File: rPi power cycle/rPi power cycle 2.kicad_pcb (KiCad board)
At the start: 2 copper layers, 53.3 x 25.4 mm, 9 parts, among them J1 RPi GPIO, J2 BATT, J3 RPi PWR, Q1 BC548

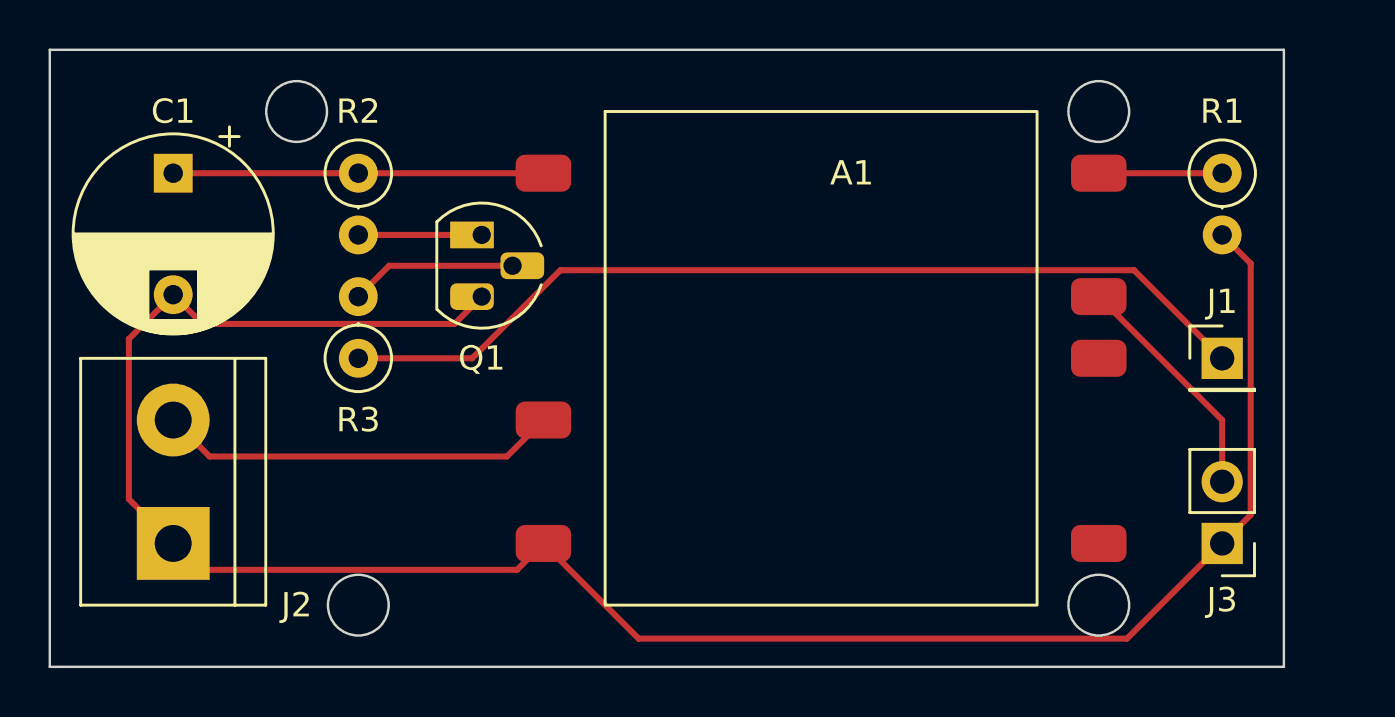
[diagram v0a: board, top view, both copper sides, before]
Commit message: Swap Q1 and R3 locations
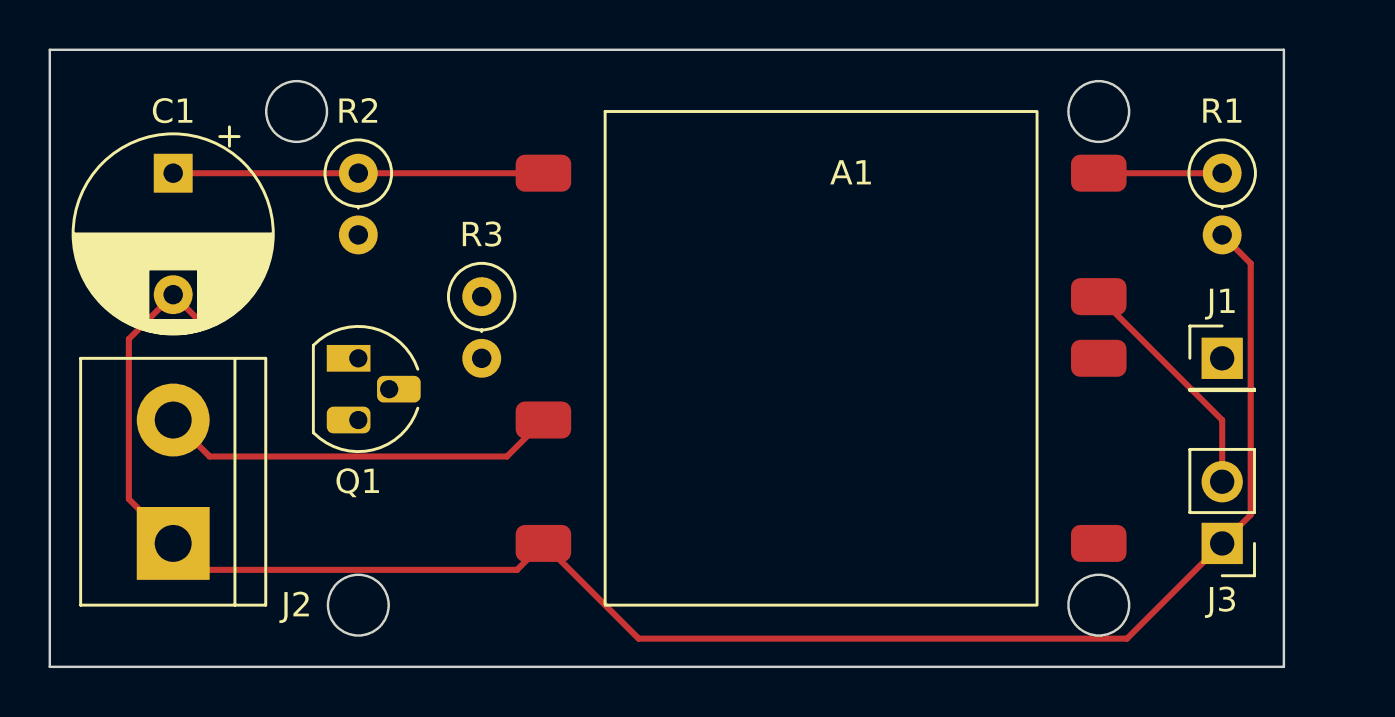
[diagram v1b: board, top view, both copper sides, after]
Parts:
- moved Q1 7.18 mm to (96.5, 88.9)
- moved R3 5.68 mm to (101.6, 86.4), turned to -90 degrees
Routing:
- net Net-(J1-Pad1): track 38.6 -> 0.00 mm
- net GND: track 86.4 -> 74.5 mm
- net Net-(Q1-Pad2): track 6.88 -> 0.00 mm
- net Net-(Q1-Pad1): track 5.08 -> 0.00 mm
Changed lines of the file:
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@@
   (net 10 "Net-(Q1-Pad2)")
   (footprint "Package_TO_SOT_THT:TO-92_HandSolder" (layer "F.Cu")
-    (at 101.6 83.82 -90)
+    (at 96.52 88.9 -90)
     (descr "TO-92 leads molded, narrow, drill 0.75mm, handsoldering variant with enlarged pads (see NXP sot054_po.pdf)")
     (tags "to-92 sc-43 sc-43a sot54 PA33 transistor")
@@
   )
   (footprint "Resistor_THT:R_Axial_DIN0207_L6.3mm_D2.5mm_P2.54mm_Vertical" (layer "F.Cu")
-    (at 96.52 88.9 90)
+    (at 101.6 86.36 -90)
     (descr "Resistor, Axial_DIN0207 series, Axial, Vertical, pin pitch=2.54mm, 0.25W = 1/4W, length*diameter=6.3*2.5mm^2, http://cdn-reichelt.de/documents/datenblatt/B400/1_4W%23YAG.pdf")
     (tags "Resistor Axial_DIN0207 series Axial Vertical pin pitch 2.54mm 0.25W = 1/4W length 6.3mm diameter 2.5mm")
@@
     (fp_line (start 0 0) (end 2.54 0) (layer "F.Fab") (width 0.1))
     (fp_circle (center 0 0) (end 1.25 0) (layer "F.Fab") (width 0.1) (fill none))
-    (pad "1" thru_hole circle (at 0 0 90) (size 1.6 1.6) (drill 0.8) (layers *.Cu *.Mask)
+    (pad "1" thru_hole circle (at 0 0 270) (size 1.6 1.6) (drill 0.8) (layers *.Cu *.Mask)
       (net 8 "Net-(J1-Pad1)") (pintype "passive"))
-    (pad "2" thru_hole oval (at 2.54 0 90) (size 1.6 1.6) (drill 0.8) (layers *.Cu *.Mask)
+    (pad "2" thru_hole oval (at 2.54 0 270) (size 1.6 1.6) (drill 0.8) (layers *.Cu *.Mask)
       (net 10 "Net-(Q1-Pad2)") (pintype "passive"))
     (model "${KICAD6_3DMODEL_DIR}/Resistor_THT.3dshapes/R_Axial_DIN0207_L6.3mm_D2.5mm_P2.54mm_Vertical.wrl"
@@
   (segment (start 104.14 96.52) (end 108.058482 100.438482) (width 0.25) (layer "F.Cu") (net 3))
   (segment (start 132.08 96.52) (end 133.254511 95.345489) (width 0.25) (layer "F.Cu") (net 3))
-  (segment (start 100.475489 87.484511) (end 90.104511 87.484511) (width 0.25) (layer "F.Cu") (net 3))
   (segment (start 88.9 96.52) (end 87.075489 94.695489) (width 0.25) (layer "F.Cu") (net 3))
   (segment (start 87.075489 88.104511) (end 88.9 86.28) (width 0.25) (layer "F.Cu") (net 3))
-  (segment (start 101.6 86.36) (end 100.475489 87.484511) (width 0.25) (layer "F.Cu") (net 3))
   (segment (start 133.254511 95.345489) (end 133.254511 84.994511) (width 0.25) (layer "F.Cu") (net 3))
   (segment (start 89.98652 97.60652) (end 103.05348 97.60652) (width 0.25) (layer "F.Cu") (net 3))
@@
   (segment (start 127 86.36) (end 132.08 91.44) (width 0.25) (layer "F.Cu") (net 6))
   (segment (start 127 81.28) (end 132.08 81.28) (width 0.25) (layer "F.Cu") (net 7))
-  (segment (start 132.08 88.9) (end 128.45348 85.27348) (width 0.25) (layer "F.Cu") (net 8))
-  (segment (start 101.207849 88.9) (end 96.52 88.9) (width 0.25) (layer "F.Cu") (net 8))
-  (segment (start 104.834369 85.27348) (end 101.207849 88.9) (width 0.25) (layer "F.Cu") (net 8))
-  (segment (start 128.45348 85.27348) (end 104.834369 85.27348) (width 0.25) (layer "F.Cu") (net 8))
-  (segment (start 101.6 83.82) (end 96.52 83.82) (width 0.25) (layer "F.Cu") (net 9))
-  (segment (start 102.87 85.09) (end 97.79 85.09) (width 0.25) (layer "F.Cu") (net 10))
-  (segment (start 97.79 85.09) (end 96.52 86.36) (width 0.25) (layer "F.Cu") (net 10))
 )

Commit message: Route tracks and cleanup
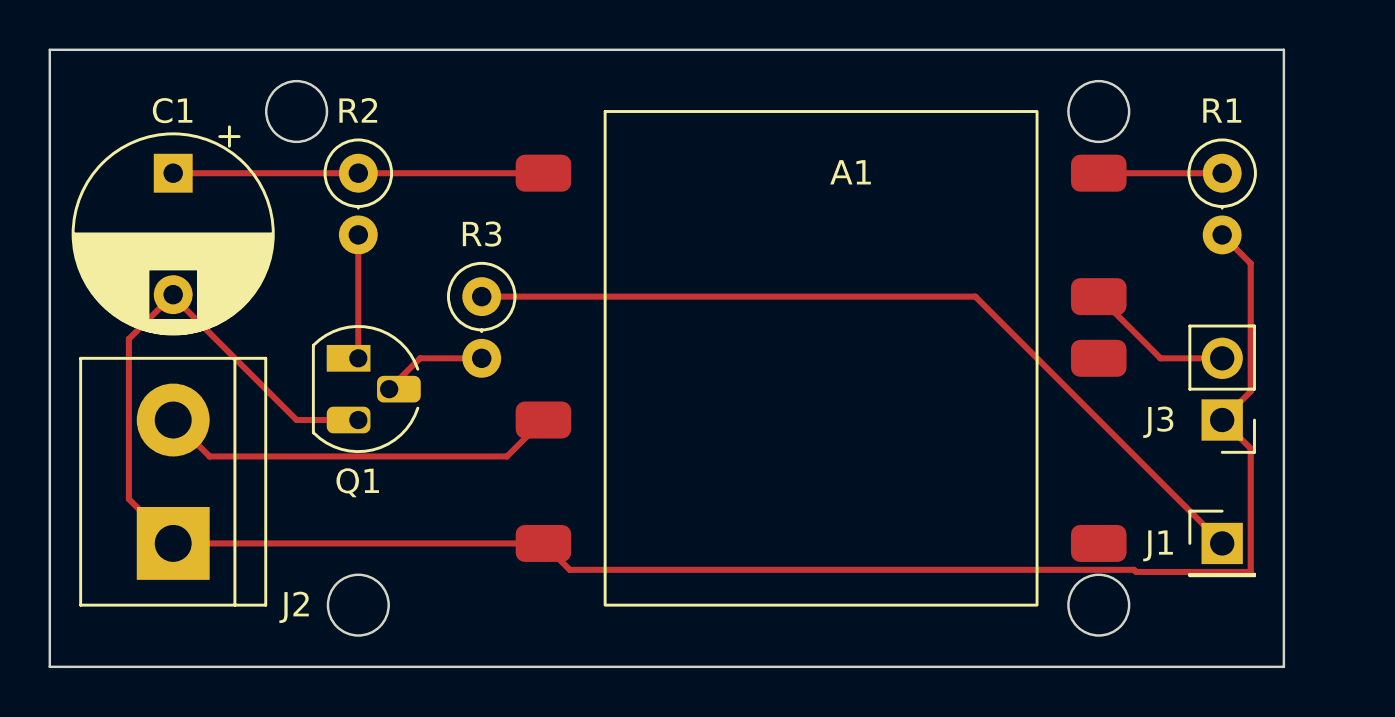
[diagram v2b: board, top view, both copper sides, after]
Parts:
- moved J1 7.62 mm to (132.1, 96.5)
- moved J3 5.08 mm to (132.1, 91.4)
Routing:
- net Net-(J1-Pad1): track 0.00 -> 34.7 mm
- net GND: track 74.5 -> 81.7 mm
- net Net-(Q1-Pad1): track 0.00 -> 5.08 mm
- net Net-(Q1-Pad2): track 0.00 -> 4.34 mm
- net +5V: track 9.72 -> 6.13 mm
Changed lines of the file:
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@@
   )
   (footprint "Connector_PinHeader_2.54mm:PinHeader_1x01_P2.54mm_Vertical" (layer "F.Cu")
-    (at 132.08 88.9)
+    (at 132.08 96.52)
     (descr "Through hole straight pin header, 1x01, 2.54mm pitch, single row")
     (tags "Through hole pin header THT 1x01 2.54mm single row")
@@
     (property "Sheetname" "")
     (attr through_hole)
-    (fp_text reference "J1" (at 0 -2.33) (layer "F.SilkS")
+    (fp_text reference "J1" (at -2.54 0) (layer "F.SilkS")
       (effects (font (size 1 1) (thickness 0.15)))
     )
@@
   )
   (footprint "Connector_PinHeader_2.54mm:PinHeader_1x02_P2.54mm_Vertical" (layer "F.Cu")
-    (at 132.08 96.52 180)
+    (at 132.08 91.44 180)
     (descr "Through hole straight pin header, 1x02, 2.54mm pitch, single row")
     (tags "Through hole pin header THT 1x02 2.54mm single row")
@@
     (property "Sheetname" "")
     (attr through_hole)
-    (fp_text reference "J3" (at 0 -2.33 180) (layer "F.SilkS")
+    (fp_text reference "J3" (at 2.54 0 180) (layer "F.SilkS")
       (effects (font (size 1 1) (thickness 0.15)))
     )
@@
   (gr_circle (center 127 78.74) (end 128.25 78.74) (layer "Edge.Cuts") (width 0.1) (fill none))
   (segment (start 88.9 81.28) (end 104.14 81.28) (width 0.25) (layer "F.Cu") (net 1))
-  (segment (start 90.4 92.94) (end 102.64 92.94) (width 0.25) (layer "F.Cu") (net 2))
+  (segment (start 102.64 92.94) (end 90.4 92.94) (width 0.25) (layer "F.Cu") (net 2))
   (segment (start 102.64 92.94) (end 104.14 91.44) (width 0.25) (layer "F.Cu") (net 2))
   (segment (start 88.9 91.44) (end 90.4 92.94) (width 0.25) (layer "F.Cu") (net 2))
-  (segment (start 108.058482 100.438482) (end 128.161518 100.438482) (width 0.25) (layer "F.Cu") (net 3))
-  (segment (start 104.14 96.52) (end 108.058482 100.438482) (width 0.25) (layer "F.Cu") (net 3))
-  (segment (start 132.08 96.52) (end 133.254511 95.345489) (width 0.25) (layer "F.Cu") (net 3))
   (segment (start 88.9 96.52) (end 87.075489 94.695489) (width 0.25) (layer "F.Cu") (net 3))
+  (segment (start 104.14 96.52) (end 105.22652 97.60652) (width 0.25) (layer "F.Cu") (net 3))
+  (segment (start 133.254511 97.694511) (end 133.254511 92.614511) (width 0.25) (layer "F.Cu") (net 3))
+  (segment (start 93.98 91.44) (end 88.9 86.36) (width 0.25) (layer "F.Cu") (net 3))
+  (segment (start 132.08 91.44) (end 133.254511 90.265489) (width 0.25) (layer "F.Cu") (net 3))
+  (segment (start 88.9 96.52) (end 104.14 96.52) (width 0.25) (layer "F.Cu") (net 3))
+  (segment (start 133.254511 90.265489) (end 133.254511 84.994511) (width 0.25) (layer "F.Cu") (net 3))
+  (segment (start 128.541471 97.694511) (end 133.254511 97.694511) (width 0.25) (layer "F.Cu") (net 3))
+  (segment (start 96.52 91.44) (end 93.98 91.44) (width 0.25) (layer "F.Cu") (net 3))
+  (segment (start 133.254511 92.614511) (end 132.08 91.44) (width 0.25) (layer "F.Cu") (net 3))
+  (segment (start 133.254511 84.994511) (end 132.08 83.82) (width 0.25) (layer "F.Cu") (net 3))
+  (segment (start 128.45348 97.60652) (end 128.541471 97.694511) (width 0.25) (layer "F.Cu") (net 3))
   (segment (start 87.075489 88.104511) (end 88.9 86.28) (width 0.25) (layer "F.Cu") (net 3))
-  (segment (start 133.254511 95.345489) (end 133.254511 84.994511) (width 0.25) (layer "F.Cu") (net 3))
-  (segment (start 89.98652 97.60652) (end 103.05348 97.60652) (width 0.25) (layer "F.Cu") (net 3))
+  (segment (start 105.22652 97.60652) (end 128.45348 97.60652) (width 0.25) (layer "F.Cu") (net 3))
   (segment (start 87.075489 94.695489) (end 87.075489 88.104511) (width 0.25) (layer "F.Cu") (net 3))
-  (segment (start 88.9 96.52) (end 89.98652 97.60652) (width 0.25) (layer "F.Cu") (net 3))
-  (segment (start 128.161518 100.438482) (end 132.08 96.52) (width 0.25) (layer "F.Cu") (net 3))
-  (segment (start 133.254511 84.994511) (end 132.08 83.82) (width 0.25) (layer "F.Cu") (net 3))
-  (segment (start 103.05348 97.60652) (end 104.14 96.52) (width 0.25) (layer "F.Cu") (net 3))
-  (segment (start 90.104511 87.484511) (end 88.9 86.28) (width 0.25) (layer "F.Cu") (net 3))
-  (segment (start 132.08 91.44) (end 132.08 93.98) (width 0.25) (layer "F.Cu") (net 6))
-  (segment (start 127 86.36) (end 132.08 91.44) (width 0.25) (layer "F.Cu") (net 6))
-  (segment (start 127 81.28) (end 132.08 81.28) (width 0.25) (layer "F.Cu") (net 7))
+  (segment (start 127 86.36) (end 129.54 88.9) (width 0.25) (layer "F.Cu") (net 6))
+  (segment (start 129.54 88.9) (end 132.08 88.9) (width 0.25) (layer "F.Cu") (net 6))
+  (segment (start 132.08 81.28) (end 127 81.28) (width 0.25) (layer "F.Cu") (net 7))
+  (segment (start 101.6 86.36) (end 121.92 86.36) (width 0.25) (layer "F.Cu") (net 8))
+  (segment (start 121.92 86.36) (end 132.08 96.52) (width 0.25) (layer "F.Cu") (net 8))
+  (segment (start 96.52 83.82) (end 96.52 88.9) (width 0.25) (layer "F.Cu") (net 9))
+  (segment (start 99.06 88.9) (end 101.6 88.9) (width 0.25) (layer "F.Cu") (net 10))
+  (segment (start 97.79 90.17) (end 99.06 88.9) (width 0.25) (layer "F.Cu") (net 10))
 )

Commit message: Straighten some traces
Shifted Q1 up a little
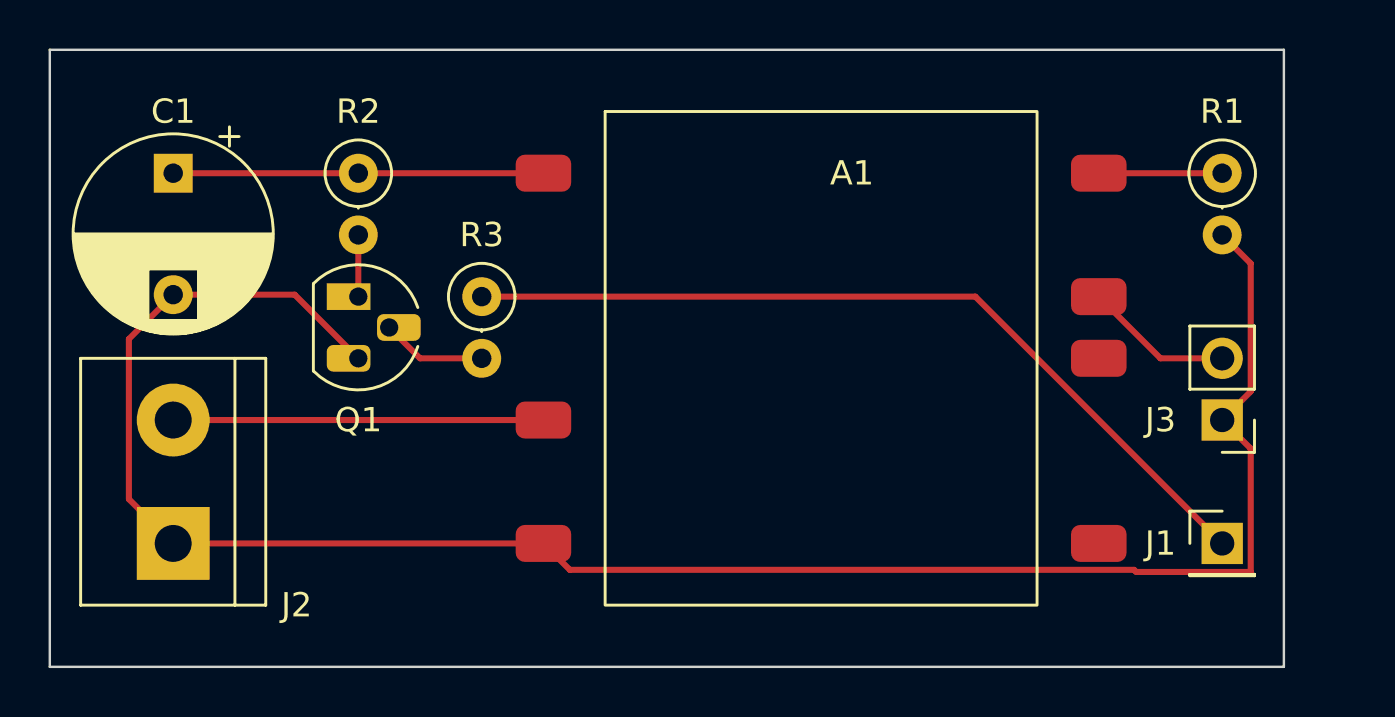
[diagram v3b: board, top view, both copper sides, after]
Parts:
- moved Q1 2.54 mm to (96.5, 86.4)
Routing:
- net Net-(Q1-Pad1): track 5.08 -> 2.54 mm
- net +12V: track 16.5 -> 15.2 mm
- net GND: track 81.7 -> 80.6 mm
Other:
- outline, holes or cut-outs redrawn
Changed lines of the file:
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@@
   (net 10 "Net-(Q1-Pad2)")
   (footprint "Package_TO_SOT_THT:TO-92_HandSolder" (layer "F.Cu")
-    (at 96.52 88.9 -90)
+    (at 96.52 86.36 -90)
     (descr "TO-92 leads molded, narrow, drill 0.75mm, handsoldering variant with enlarged pads (see NXP sot054_po.pdf)")
     (tags "to-92 sc-43 sc-43a sot54 PA33 transistor")
@@
   (gr_circle (center 137.16 81.28) (end 137.16 81.28) (layer "Edge.Cuts") (width 0.1) (fill none))
   (gr_rect (start 83.82 76.2) (end 134.62 101.6) (layer "Edge.Cuts") (width 0.1) (fill none))
-  (gr_circle (center 127 99.06) (end 128.25 99.06) (layer "Edge.Cuts") (width 0.1) (fill none))
-  (gr_circle (center 93.98 78.74) (end 95.23 78.74) (layer "Edge.Cuts") (width 0.1) (fill none))
-  (gr_circle (center 96.52 99.06) (end 97.77 99.06) (layer "Edge.Cuts") (width 0.1) (fill none))
-  (gr_circle (center 127 78.74) (end 128.25 78.74) (layer "Edge.Cuts") (width 0.1) (fill none))
   (segment (start 88.9 81.28) (end 104.14 81.28) (width 0.25) (layer "F.Cu") (net 1))
-  (segment (start 102.64 92.94) (end 90.4 92.94) (width 0.25) (layer "F.Cu") (net 2))
-  (segment (start 102.64 92.94) (end 104.14 91.44) (width 0.25) (layer "F.Cu") (net 2))
-  (segment (start 88.9 91.44) (end 90.4 92.94) (width 0.25) (layer "F.Cu") (net 2))
+  (segment (start 104.14 91.44) (end 88.9 91.44) (width 0.25) (layer "F.Cu") (net 2))
   (segment (start 88.9 96.52) (end 87.075489 94.695489) (width 0.25) (layer "F.Cu") (net 3))
   (segment (start 104.14 96.52) (end 105.22652 97.60652) (width 0.25) (layer "F.Cu") (net 3))
+  (segment (start 88.9 86.28) (end 93.9 86.28) (width 0.25) (layer "F.Cu") (net 3))
   (segment (start 133.254511 97.694511) (end 133.254511 92.614511) (width 0.25) (layer "F.Cu") (net 3))
-  (segment (start 93.98 91.44) (end 88.9 86.36) (width 0.25) (layer "F.Cu") (net 3))
   (segment (start 132.08 91.44) (end 133.254511 90.265489) (width 0.25) (layer "F.Cu") (net 3))
   (segment (start 88.9 96.52) (end 104.14 96.52) (width 0.25) (layer "F.Cu") (net 3))
   (segment (start 133.254511 90.265489) (end 133.254511 84.994511) (width 0.25) (layer "F.Cu") (net 3))
   (segment (start 128.541471 97.694511) (end 133.254511 97.694511) (width 0.25) (layer "F.Cu") (net 3))
-  (segment (start 96.52 91.44) (end 93.98 91.44) (width 0.25) (layer "F.Cu") (net 3))
   (segment (start 133.254511 92.614511) (end 132.08 91.44) (width 0.25) (layer "F.Cu") (net 3))
   (segment (start 133.254511 84.994511) (end 132.08 83.82) (width 0.25) (layer "F.Cu") (net 3))
   (segment (start 128.45348 97.60652) (end 128.541471 97.694511) (width 0.25) (layer "F.Cu") (net 3))
   (segment (start 87.075489 88.104511) (end 88.9 86.28) (width 0.25) (layer "F.Cu") (net 3))
+  (segment (start 93.9 86.28) (end 96.52 88.9) (width 0.25) (layer "F.Cu") (net 3))
   (segment (start 105.22652 97.60652) (end 128.45348 97.60652) (width 0.25) (layer "F.Cu") (net 3))
   (segment (start 87.075489 94.695489) (end 87.075489 88.104511) (width 0.25) (layer "F.Cu") (net 3))
@@
   (segment (start 101.6 86.36) (end 121.92 86.36) (width 0.25) (layer "F.Cu") (net 8))
   (segment (start 121.92 86.36) (end 132.08 96.52) (width 0.25) (layer "F.Cu") (net 8))
-  (segment (start 96.52 83.82) (end 96.52 88.9) (width 0.25) (layer "F.Cu") (net 9))
+  (segment (start 96.52 83.82) (end 96.52 86.36) (width 0.25) (layer "F.Cu") (net 9))
+  (segment (start 97.79 87.63) (end 99.06 88.9) (width 0.25) (layer "F.Cu") (net 10))
   (segment (start 99.06 88.9) (end 101.6 88.9) (width 0.25) (layer "F.Cu") (net 10))
-  (segment (start 97.79 90.17) (end 99.06 88.9) (width 0.25) (layer "F.Cu") (net 10))
 )
